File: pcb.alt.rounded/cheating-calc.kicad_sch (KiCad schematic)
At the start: 8 parts, among them J1 Conn_01x04, Q1 MMBF170, Q2 MMBF170, U1 XIAO-ESP32-S3-SMD

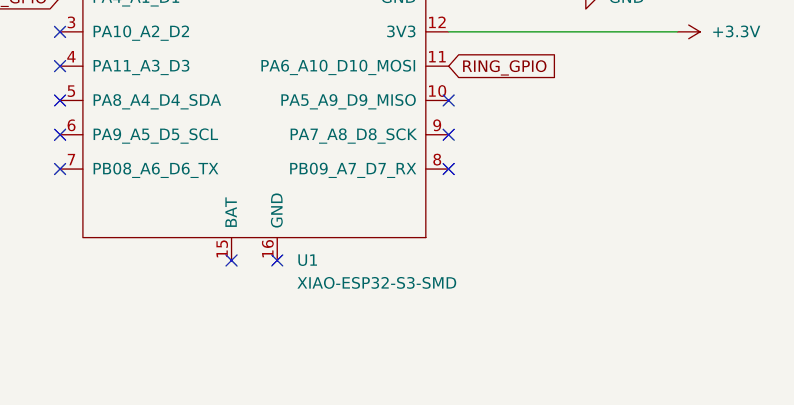
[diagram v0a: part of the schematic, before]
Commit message: tweak silkscreen and schematic
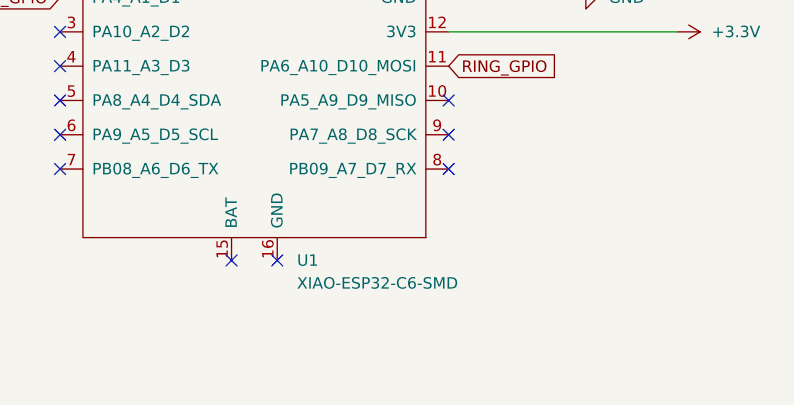
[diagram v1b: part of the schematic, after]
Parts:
- U1: value XIAO-ESP32-S3-SMD -> XIAO-ESP32-C6-SMD
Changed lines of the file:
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@@
 			)
 		)
-		(property "Value" "XIAO-ESP32-S3-SMD"
+		(property "Value" "XIAO-ESP32-C6-SMD"
 			(at 183.8041 113.03 0)
 			(effects
